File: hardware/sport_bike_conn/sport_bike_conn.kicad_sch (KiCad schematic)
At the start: 5 parts, among them J1 to_bike_computer, J2 from_reed_switch

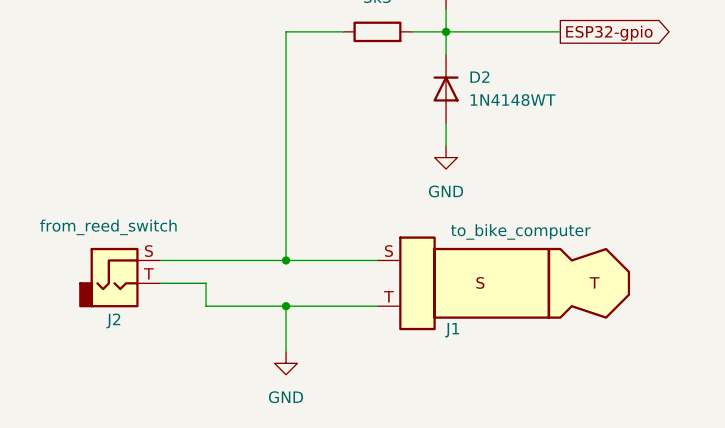
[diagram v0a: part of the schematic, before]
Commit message: Fix hw circuit connections
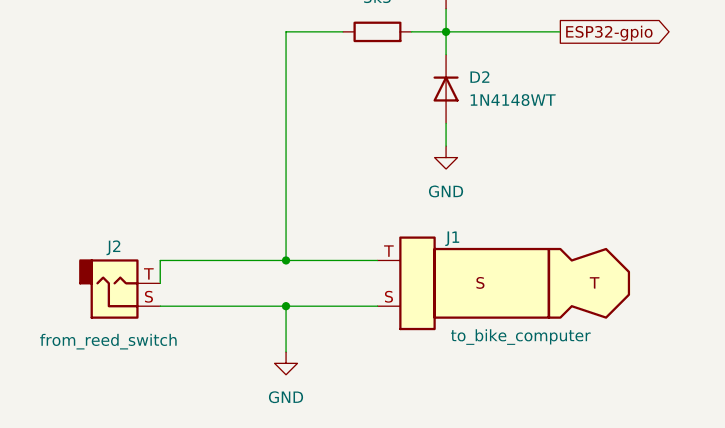
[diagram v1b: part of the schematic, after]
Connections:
- net GND: now also J1.S, J2.S; no longer J1.T, J2.T
- new net: J1.T, J2.T, R1.1
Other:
- moved on the sheet: J1, J2
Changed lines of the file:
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@@
 	(paper "A4")
+	(junction
+		(at 110.49 81.28)
+		(diameter 0)
+		(color 0 0 0 0)
+	)
 	(junction
 		(at 128.27 50.8)
@@
 		(color 0 0 0 0)
 	)
-	(junction
-		(at 110.49 81.28)
-		(diameter 0)
-		(color 0 0 0 0)
-	)
 	(wire
 		(pts
@@
 	(wire
 		(pts
-			(xy 110.49 81.28) (xy 101.6 81.28)
+			(xy 96.52 76.2) (xy 110.49 76.2)
 		)
 		(stroke
@@
 	(wire
 		(pts
-			(xy 101.6 81.28) (xy 101.6 78.74)
-		)
-		(stroke
-			(width 0)
-			(type default)
-		)
-	)
-	(wire
-		(pts
-			(xy 120.65 81.28) (xy 110.49 81.28)
+			(xy 110.49 50.8) (xy 110.49 76.2)
 		)
 		(stroke
@@
 	(wire
 		(pts
-			(xy 110.49 50.8) (xy 110.49 76.2)
-		)
-		(stroke
-			(width 0)
-			(type default)
-		)
-	)
-	(wire
-		(pts
-			(xy 96.52 78.74) (xy 101.6 78.74)
-		)
-		(stroke
-			(width 0)
-			(type default)
-		)
-	)
-	(wire
-		(pts
-			(xy 96.52 76.2) (xy 110.49 76.2)
+			(xy 110.49 76.2) (xy 120.65 76.2)
+		)
+		(stroke
+			(width 0)
+			(type default)
+		)
+	)
+	(wire
+		(pts
+			(xy 96.52 81.28) (xy 110.49 81.28)
 		)
 		(stroke
@@
 	(wire
 		(pts
+			(xy 96.52 76.2) (xy 96.52 78.74)
+		)
+		(stroke
+			(width 0)
+			(type default)
+		)
+	)
+	(wire
+		(pts
+			(xy 110.49 81.28) (xy 120.65 81.28)
+		)
+		(stroke
+			(width 0)
+			(type default)
+		)
+	)
+	(wire
+		(pts
 			(xy 124.46 50.8) (xy 128.27 50.8)
-		)
-		(stroke
-			(width 0)
-			(type default)
-		)
-	)
-	(wire
-		(pts
-			(xy 110.49 76.2) (xy 120.65 76.2)
 		)
 		(stroke
@@
 		(lib_id "Connector_Audio:AudioJack2")
 		(at 91.44 78.74 0)
+		(mirror x)
 		(unit 1)
 		(exclude_from_sim no)
@@
 		(dnp no)
 		(property "Reference" "J2"
-			(at 91.44 82.804 0)
+			(at 91.44 74.676 0)
 			(effects
 				(font
@@
 		)
 		(property "Value" "from_reed_switch"
-			(at 90.805 72.39 0)
+			(at 90.805 85.09 0)
 			(effects
 				(font
@@
 	(symbol
 		(lib_id "Connector_Audio:AudioPlug2")
-		(at 135.89 78.74 0)
-		(mirror y)
+		(at 135.89 78.74 180)
 		(unit 1)
 		(exclude_from_sim no)
@@
 		(dnp no)
 		(property "Reference" "J1"
-			(at 128.27 83.82 0)
+			(at 128.27 73.66 0)
 			(effects
 				(font
@@
 		)
 		(property "Value" "to_bike_computer"
-			(at 128.778 72.898 0)
+			(at 128.778 84.582 0)
 			(effects
 				(font
@@
 		)
 		(property "Footprint" ""
-			(at 127 80.01 0)
+			(at 127 77.47 0)
 			(effects
 				(font
@@
 		)
 		(property "Datasheet" "~"
-			(at 127 80.01 0)
-			(effects
-				(font
+			(at 127 77.47 0)
+			(effects
+				(font

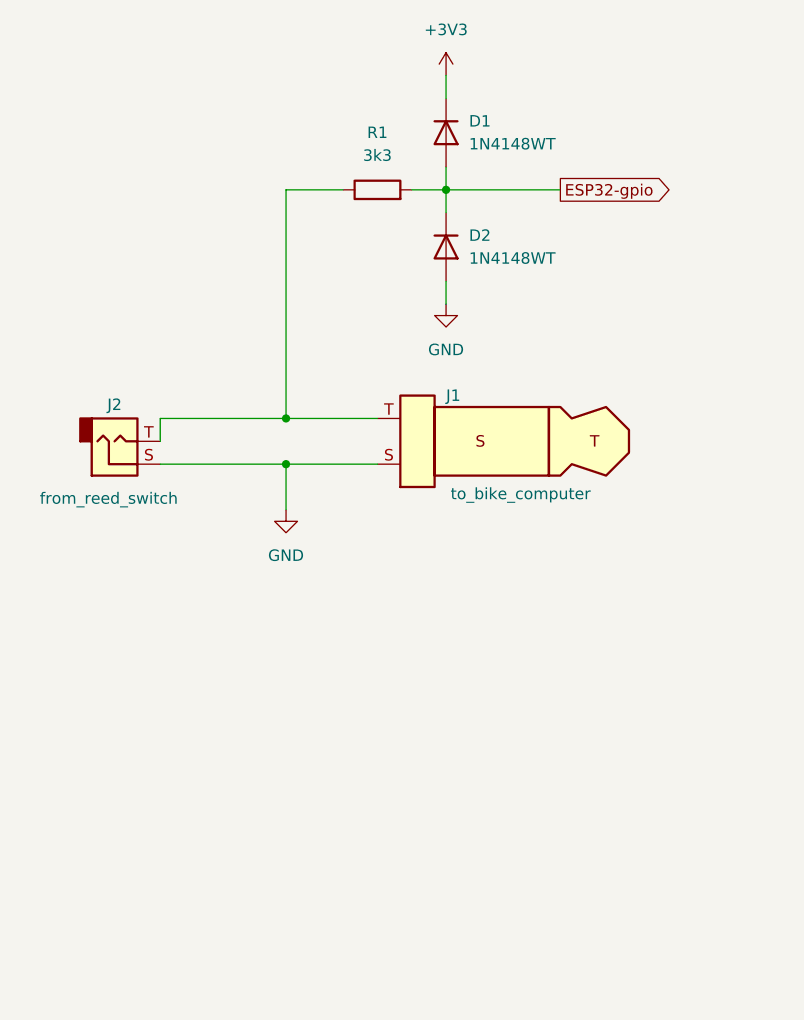
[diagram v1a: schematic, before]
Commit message: Update README.md and images.
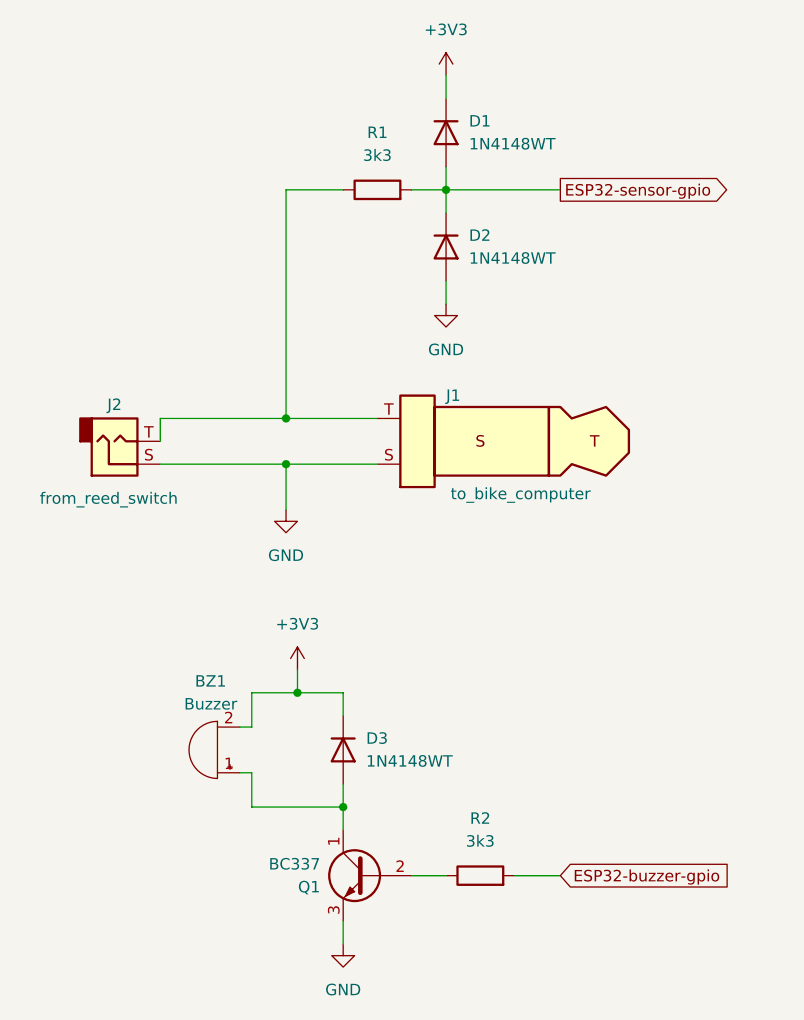
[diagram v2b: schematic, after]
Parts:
- added BZ1: Buzzer, symbol Device:Buzzer
- added D3: 1N4148WT, Diode_SMD:D_SOD-523, symbol Diode:1N4148WT
- added Q1: BC337, Package_TO_SOT_THT:TO-92_Inline, symbol Transistor_BJT:BC337
- added R2: 3k3, symbol Device:R
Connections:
- net +3V3: now also BZ1.2 (-), D3.1 (K)
- net GND: now also Q1.3 (E)
- net ESP32-gpio renamed ESP32-sensor-gpio
- new net: BZ1.1 (+), D3.2 (A), Q1.1 (C)
- new net: Q1.2 (B), R2.1
- new net ESP32-buzzer-gpio: R2.2
